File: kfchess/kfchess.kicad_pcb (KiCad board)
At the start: 2 copper layers, 260 x 220 mm, 232 parts, among them Q1 AO3400A, Q10 AO3400A, Q11 AO3400A, Q12 AO3400A, Q13 AO3400A, Q14 AO3400A, Q15 AO3400A, Q16 AO3400A, Q2 AO3400A, Q3 AO3400A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

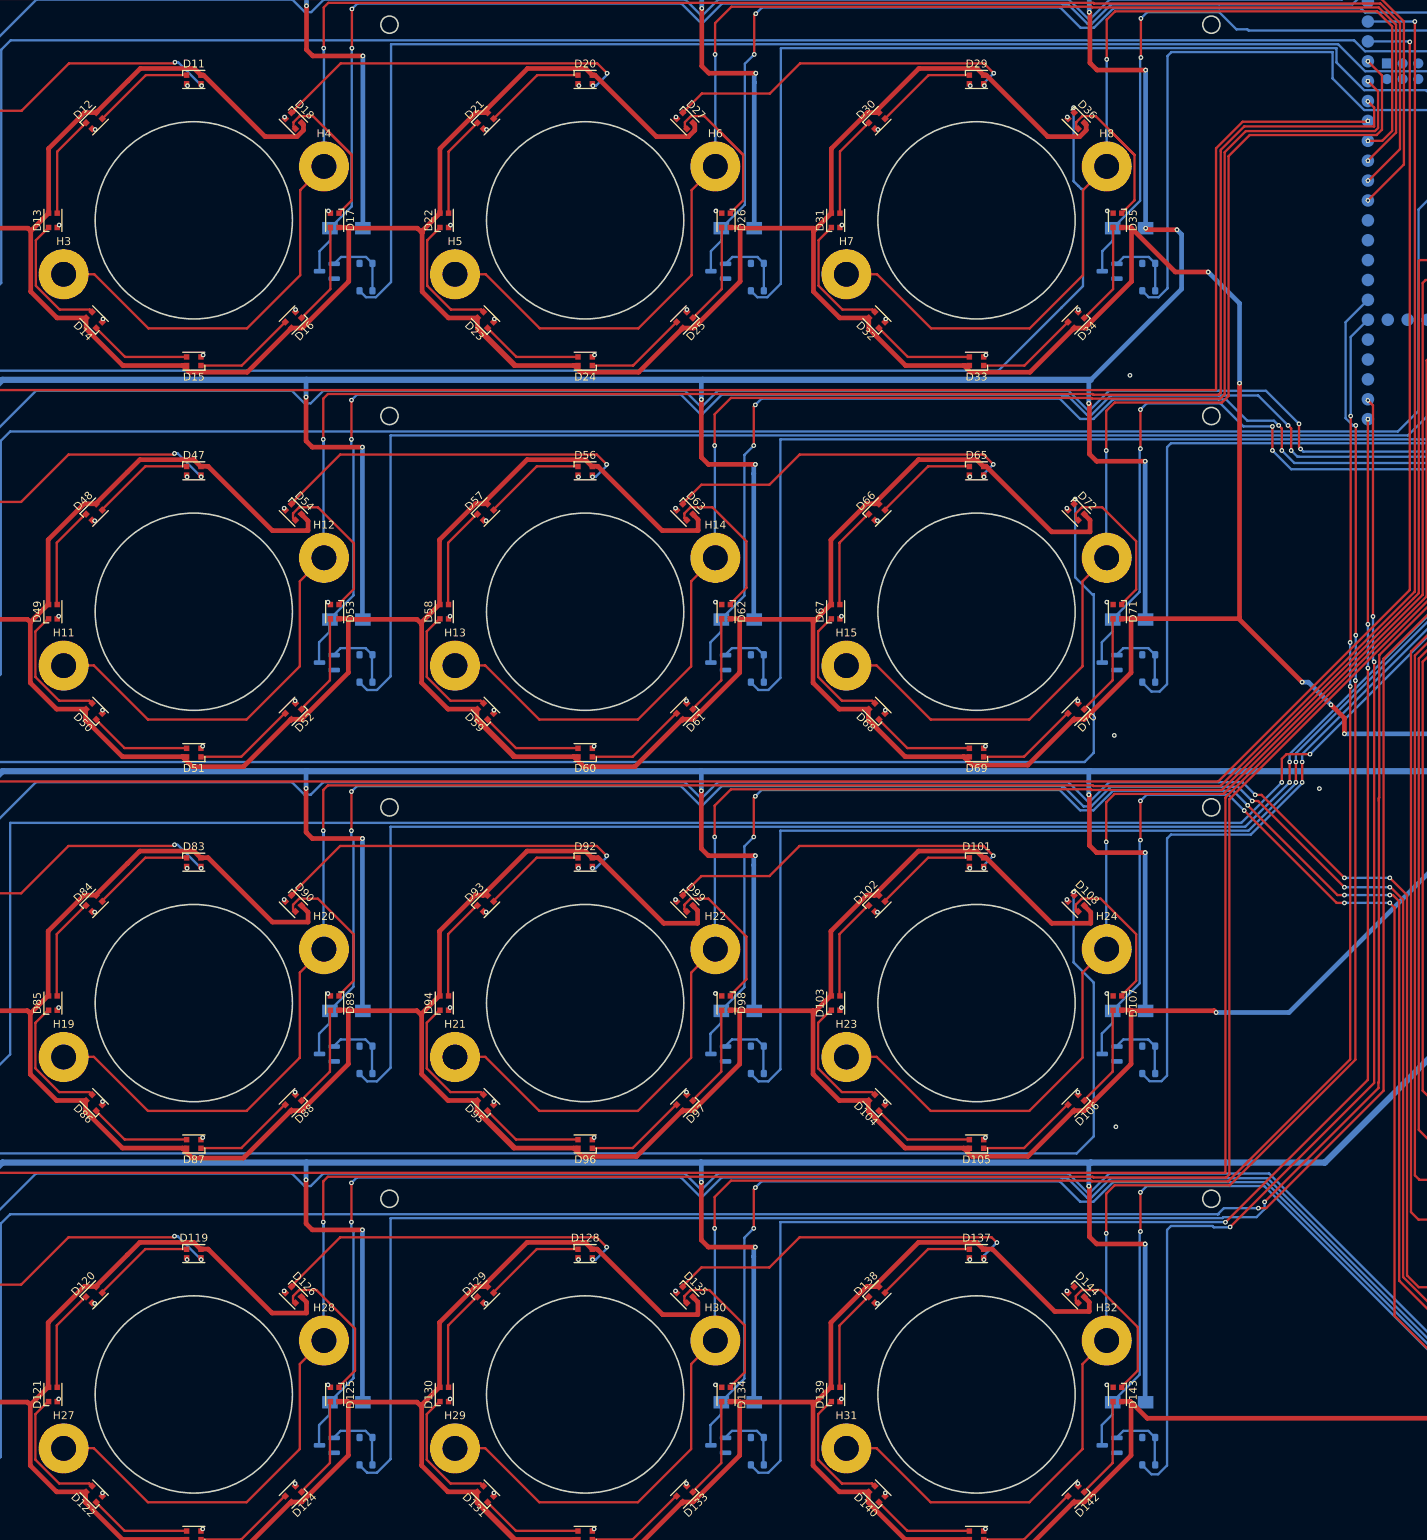
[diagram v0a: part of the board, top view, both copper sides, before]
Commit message: Got ws2812 leds working
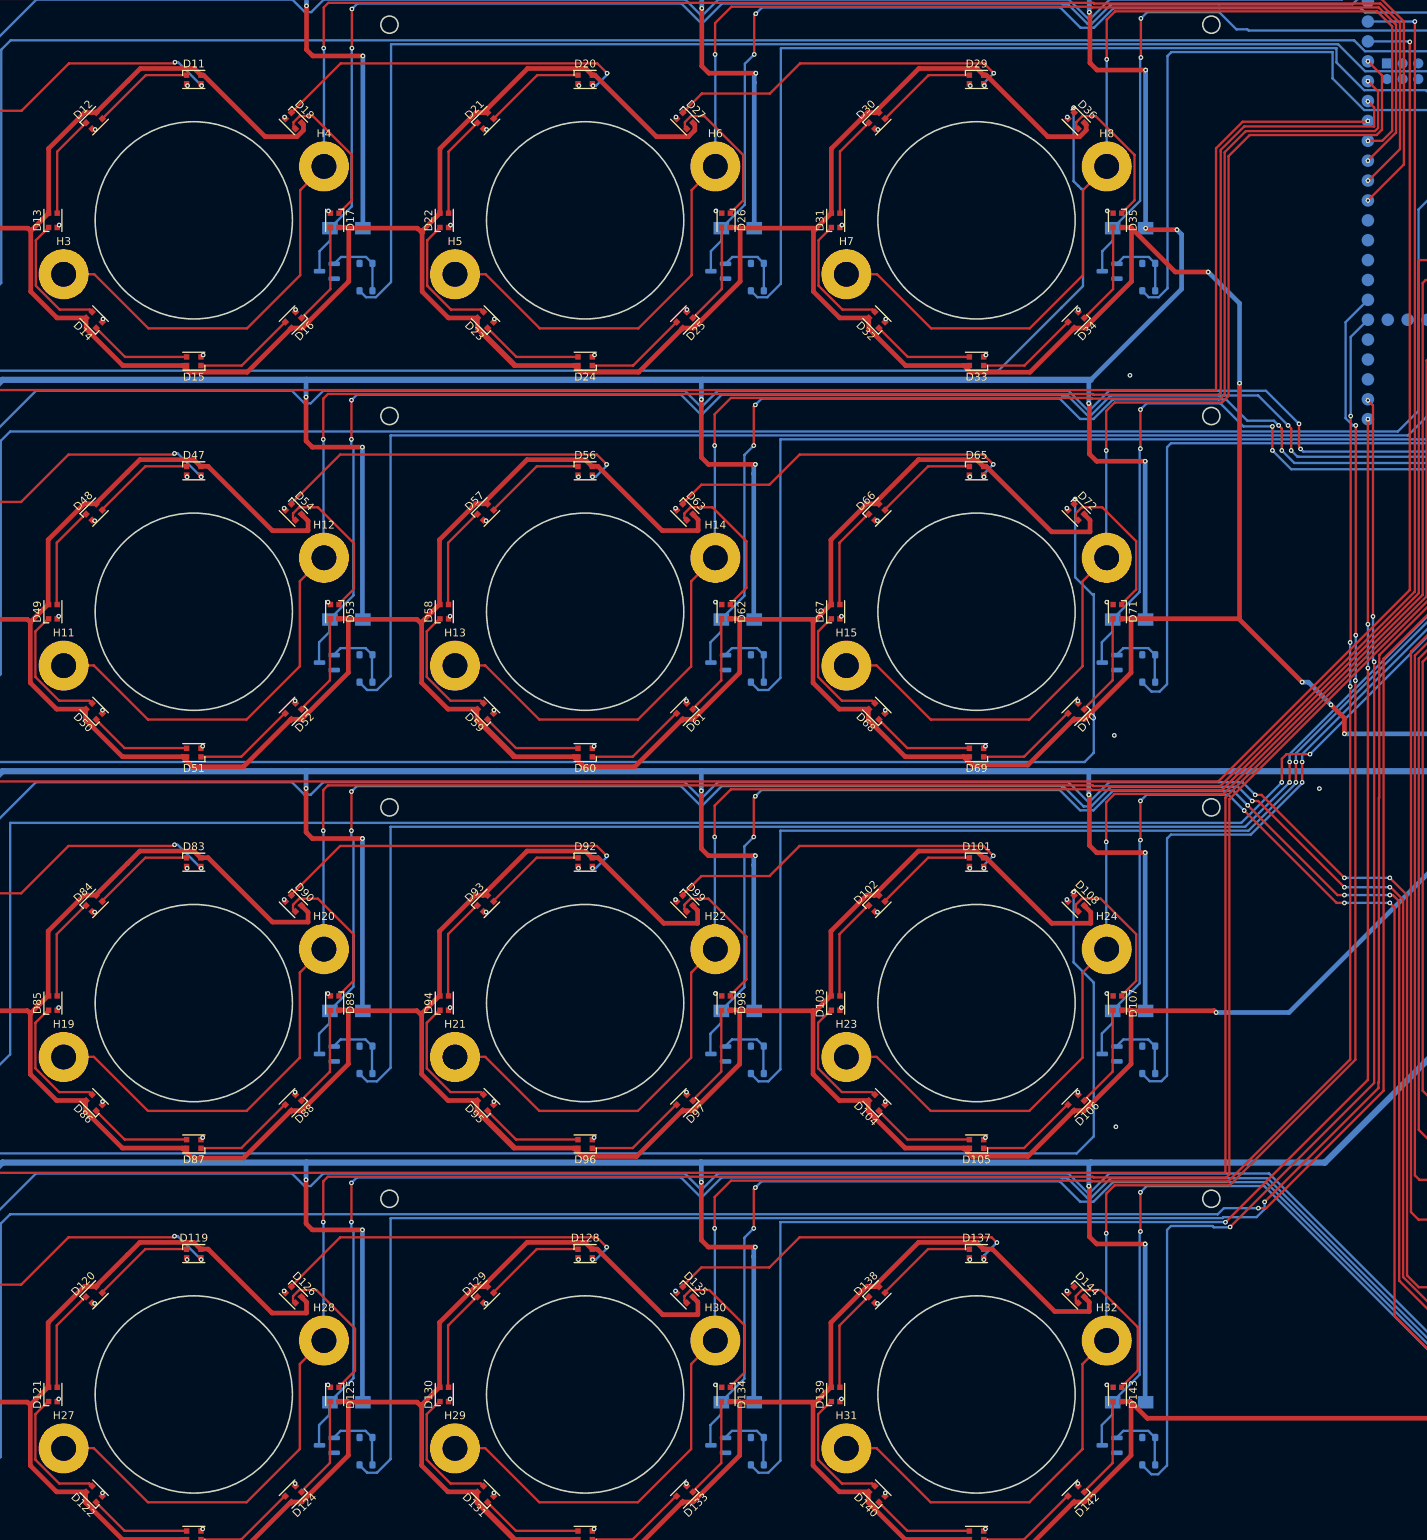
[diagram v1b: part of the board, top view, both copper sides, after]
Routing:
- net +5V: track 2682.8 -> 2604.4 mm
- net Net-(D35-DOUT): track 23.2 -> 18.9 mm
- net Net-(D26-DOUT): track 23.2 -> 18.9 mm
- net Net-(D17-DOUT): track 23.2 -> 18.9 mm
- net /s42: track 311.4 -> 310.4 mm
- net /s32: track 301.2 -> 300.2 mm
- net /s22: track 242.8 -> 241.8 mm
- net /s12: track 233.0 -> 232.1 mm
